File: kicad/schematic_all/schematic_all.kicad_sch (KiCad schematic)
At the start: 43 parts, among them SW1 Button 1, SW2 Encoder 1, SW3 Button 2, SW4 Encoder 2, SW5 Button 3, U1 L7805, U2 RPi_Pico, U3 RDA5807M_Module, U4 LM386

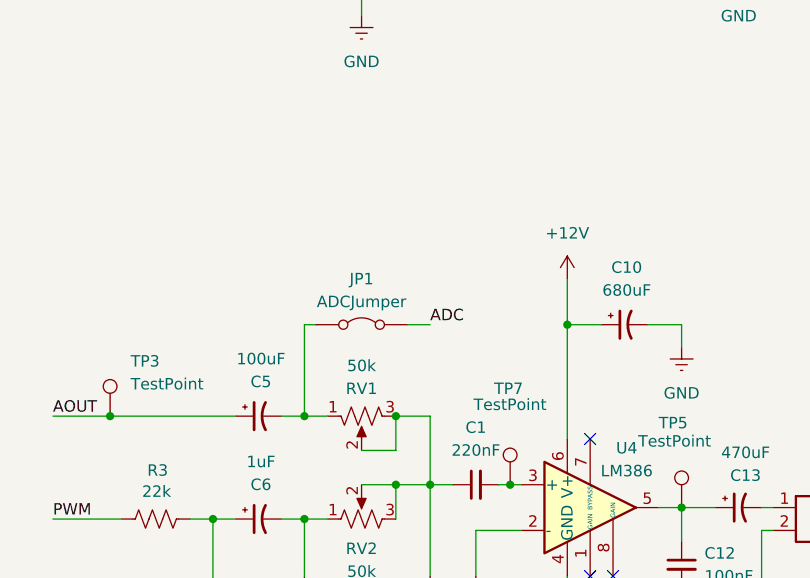
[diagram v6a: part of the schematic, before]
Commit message: replace ADC jumper with voltage divider
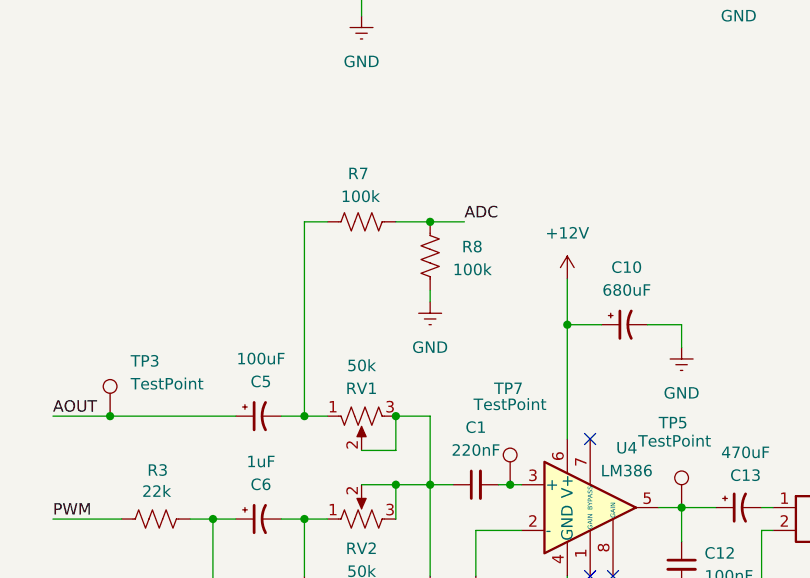
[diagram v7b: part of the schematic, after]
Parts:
- removed JP1: ADCJumper, Connector_PinHeader_2.54mm:PinHeader_1x02_P2.54mm_Vertical, symbol Jumper:Jumper_2_Bridged
- added R7, R8: 100k, Resistor_THT:R_Axial_DIN0207_L6.3mm_D2.5mm_P10.16mm_Horizontal, symbol Device:R_US
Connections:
- net ADC: now also R7.1, R8.2
- net GND: now also R8.1
- net at C5.2, RV1.1: now also R7.2
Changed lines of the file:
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@@
 	)
 	(junction
+		(at 223.52 97.79)
+		(diameter 0)
+		(color 0 0 0 0)
+	)
+	(junction
 		(at 251.46 129.54)
 		(diameter 0)
@@
 	(wire
 		(pts
-			(xy 220.98 109.22) (xy 223.52 109.22)
-		)
-		(stroke
-			(width 0)
-			(type default)
-		)
-	)
-	(wire
-		(pts
 			(xy 247.65 109.22) (xy 251.46 109.22)
 		)
@@
 	(wire
 		(pts
-			(xy 209.55 109.22) (xy 210.82 109.22)
+			(xy 209.55 97.79) (xy 212.09 97.79)
 		)
 		(stroke
@@
 	(wire
 		(pts
+			(xy 219.71 97.79) (xy 223.52 97.79)
+		)
+		(stroke
+			(width 0)
+			(type default)
+		)
+	)
+	(wire
+		(pts
 			(xy 31.75 68.58) (xy 31.75 72.39)
 		)
@@
 	(wire
 		(pts
+			(xy 223.52 97.79) (xy 227.33 97.79)
+		)
+		(stroke
+			(width 0)
+			(type default)
+		)
+	)
+	(wire
+		(pts
 			(xy 86.36 121.92) (xy 86.36 111.76)
 		)
@@
 	(wire
 		(pts
+			(xy 223.52 105.41) (xy 223.52 106.68)
+		)
+		(stroke
+			(width 0)
+			(type default)
+		)
+	)
+	(wire
+		(pts
 			(xy 110.49 93.98) (xy 113.03 93.98)
 		)
@@
 	(wire
 		(pts
-			(xy 209.55 119.38) (xy 209.55 109.22)
+			(xy 209.55 119.38) (xy 209.55 97.79)
 		)
 		(stroke
@@
 	)
 	(label "ADC"
-		(at 223.52 109.22 0)
+		(at 227.33 97.79 0)
 		(fields_autoplaced yes)
 		(effects
@@
 	)
 	(symbol
-		(lib_id "Jumper:Jumper_2_Bridged")
-		(at 215.9 109.22 0)
-		(unit 1)
-		(exclude_from_sim yes)
-		(in_bom yes)
-		(on_board yes)
-		(dnp no)
-		(fields_autoplaced yes)
-		(property "Reference" "JP1"
-			(at 215.9 104.14 0)
-			(effects
-				(font
-					(size 1.27 1.27)
-				)
-			)
-		)
-		(property "Value" "ADCJumper"
-			(at 215.9 106.68 0)
-			(effects
-				(font
-					(size 1.27 1.27)
-				)
-			)
-		)
-		(property "Footprint" "Connector_PinHeader_2.54mm:PinHeader_1x02_P2.54mm_Vertical"
-			(at 215.9 109.22 0)
-			(effects
-				(font
-					(size 1.27 1.27)
-				)
-				(hide yes)
-			)
-		)
-		(property "Datasheet" "~"
-			(at 215.9 109.22 0)
-			(effects
-				(font
-					(size 1.27 1.27)
-				)
-				(hide yes)
-			)
-		)
-		(property "Description" "Jumper, 2-pole, closed/bridged"
-			(at 215.9 109.22 0)
-			(effects
-				(font
-					(size 1.27 1.27)
-				)
-				(hide yes)
-			)
-		)
-		(pin "1"
-		)
-		(pin "2"
-		)
-		(instances
-			(project ""
-				(path "/017a32bd-a431-4565-87b4-2161296abf15"
-					(reference "JP1")
-					(unit 1)
-				)
-			)
-		)
-	)
-	(symbol
 		(lib_id "power:Earth")
 		(at 215.9 74.93 0)
@@
 	)
 	(symbol
+		(lib_id "power:Earth")
+		(at 223.52 106.68 0)
+		(unit 1)
+		(exclude_from_sim no)
+		(in_bom yes)
+		(on_board yes)
+		(dnp no)
+		(fields_autoplaced yes)
+		(property "Reference" "#PWR035"
+			(at 223.52 113.03 0)
+			(effects
+				(font
+					(size 1.27 1.27)
+				)
+				(hide yes)
+			)
+		)
+		(property "Value" "GND"
+			(at 223.52 111.76 0)
+			(effects
+				(font
+					(size 1.27 1.27)
+				)
+			)
+		)
+		(property "Footprint" ""
+			(at 223.52 106.68 0)
+			(effects
+				(font
+					(size 1.27 1.27)
+				)
+				(hide yes)
+			)
+		)
+		(property "Datasheet" "~"
+			(at 223.52 106.68 0)
+			(effects
+				(font
+					(size 1.27 1.27)
+				)
+				(hide yes)
+			)
+		)
+		(property "Description" "Power symbol creates a global label with name \"Earth\""
+			(at 223.52 106.68 0)
+			(effects
+				(font
+					(size 1.27 1.27)
+				)
+				(hide yes)
+			)
+		)
+		(pin "1"
+		)
+		(instances
+			(project "schematic_all"
+				(path "/017a32bd-a431-4565-87b4-2161296abf15"
+					(reference "#PWR035")
+					(unit 1)
+				)
+			)
+		)
+	)
+	(symbol
 		(lib_id "Connector:TestPoint")
 		(at 29.21 24.13 270)
@@
 	)
 	(symbol
+		(lib_id "Device:R_US")
+		(at 223.52 101.6 180)
+		(unit 1)
+		(exclude_from_sim no)
+		(in_bom yes)
+		(on_board yes)
+		(dnp no)
+		(property "Reference" "R8"
+			(at 229.362 100.584 0)
+			(effects
+				(font
+					(size 1.27 1.27)
+				)
+				(justify left)
+			)
+		)
+		(property "Value" "100k"
+			(at 230.378 103.124 0)
+			(effects
+				(font
+					(size 1.27 1.27)
+				)
+				(justify left)
+			)
+		)
+		(property "Footprint" "Resistor_THT:R_Axial_DIN0207_L6.3mm_D2.5mm_P10.16mm_Horizontal"
+			(at 222.504 101.346 90)
+			(effects
+				(font
+					(size 1.27 1.27)
+				)
+				(hide yes)
+			)
+		)
+		(property "Datasheet" "~"
+			(at 223.52 101.6 0)
+			(effects
+				(font
+					(size 1.27 1.27)
+				)
+				(hide yes)
+			)
+		)
+		(property "Description" "Resistor, US symbol"
+			(at 223.52 101.6 0)
+			(effects
+				(font
+					(size 1.27 1.27)
+				)
+				(hide yes)
+			)
+		)
+		(pin "1"
+		)
+		(pin "2"
+		)
+		(instances
+			(project "schematic_all"
+				(path "/017a32bd-a431-4565-87b4-2161296abf15"
+					(reference "R8")
+					(unit 1)
+				)
+			)
+		)
+	)
+	(symbol
 		(lib_id "Device:C_Polarized_Small_US")
 		(at 170.18 71.12 0)
@@
 					(unit 1)
 				)
+			)
+		)
+	)
+	(symbol
+		(lib_id "Device:R_US")
+		(at 215.9 97.79 270)
+		(unit 1)
+		(exclude_from_sim no)
+		(in_bom yes)
+		(on_board yes)
+		(dnp no)
+		(property "Reference" "R7"
+			(at 214.376 92.456 90)
+			(effects
+				(font
+					(size 1.27 1.27)
+				)
+				(justify left)
+			)
+		)
+		(property "Value" "100k"
+			(at 213.614 94.996 90)
+			(effects
+				(font
+					(size 1.27 1.27)
+				)
+				(justify left)
+			)
+		)
+		(property "Footprint" "Resistor_THT:R_Axial_DIN0207_L6.3mm_D2.5mm_P10.16mm_Horizontal"
+			(at 215.646 98.806 90)
+			(effects
+				(font
+					(size 1.27 1.27)
+				)
+				(hide yes)
+			)
+		)
+		(property "Datasheet" "~"
+			(at 215.9 97.79 0)
+			(effects
+				(font
+					(size 1.27 1.27)
+				)
+				(hide yes)
+			)
+		)
+		(property "Description" "Resistor, US symbol"
+			(at 215.9 97.79 0)
+			(effects
+				(font
+					(size 1.27 1.27)
+				)
+				(hide yes)
+			)
+		)
+		(pin "1"
+		)
+		(pin "2"
+		)
+		(instances
+			(project "schematic_all"
+				(path "/017a32bd-a431-4565-87b4-2161296abf15"
+					(reference "R7")
+					(unit 1)
+				)

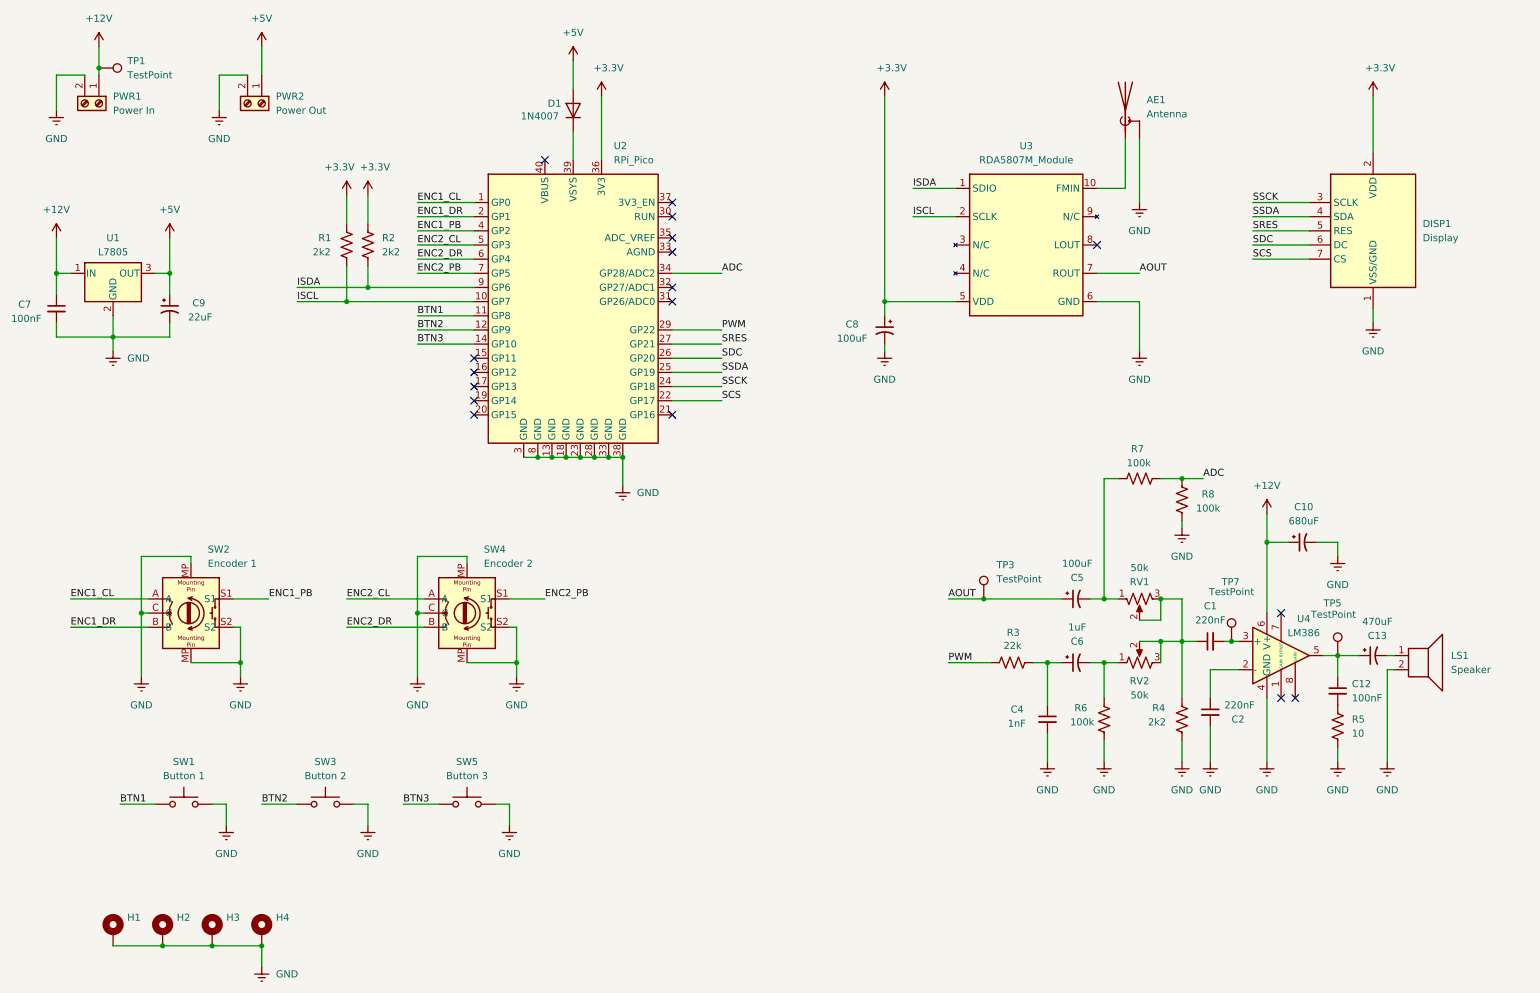
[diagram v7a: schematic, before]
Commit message: move ADC from after C5 to after C13
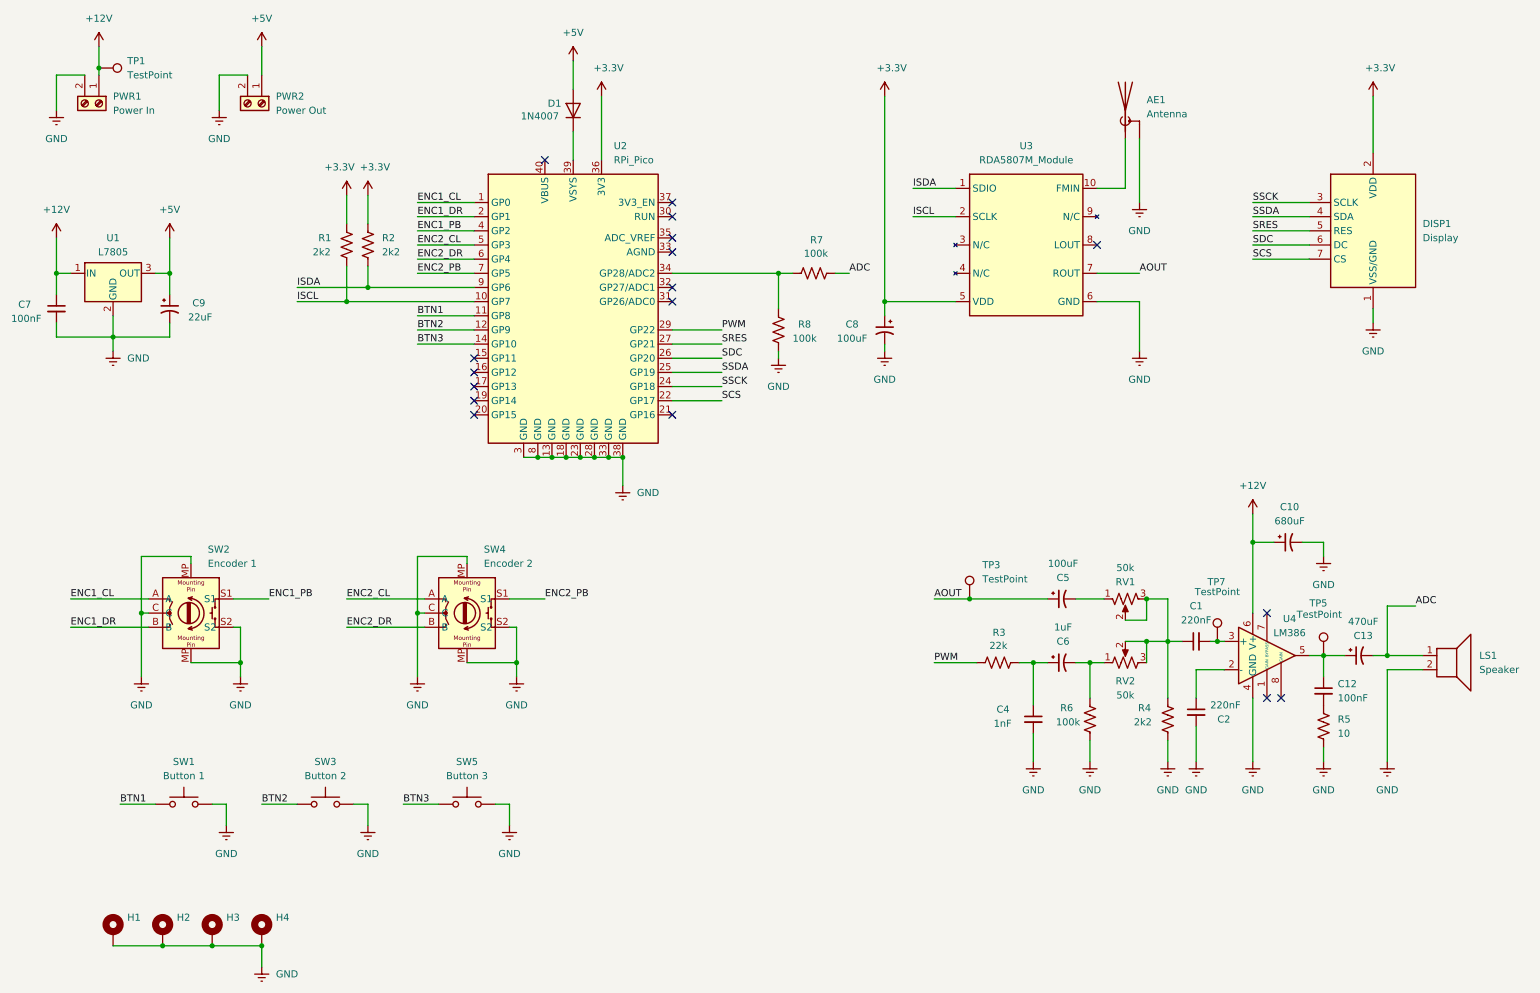
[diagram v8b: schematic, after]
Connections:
- net ADC: now also C13.2, LS1.1, R7.2; no longer R7.1, R8.2, U2.34 (GP28/ADC2)
- net at C5.2, RV1.1: no longer R7.2
- new net: R7.1, R8.2, U2.34 (GP28/ADC2)
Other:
- moved on the sheet: C1, C10, C12, C13, C2, C4, C5, C6, LS1, R3, R4, R5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
